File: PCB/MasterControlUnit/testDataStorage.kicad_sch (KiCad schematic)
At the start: 11 parts, among them U10 APS6404L-3SQR-SN, U11 APS6404L-3SQR-SN, U12 APS6404L-3SQR-SN, U2 APS6404L-3SQR-SN, U3 APS6404L-3SQR-SN, U4 APS6404L-3SQR-SN, U5 LD1117S33TR_SOT223, U6 APS6404L-3SQR-SN, U7 APS6404L-3SQR-SN, U8 APS6404L-3SQR-SN, U9 APS6404L-3SQR-SN

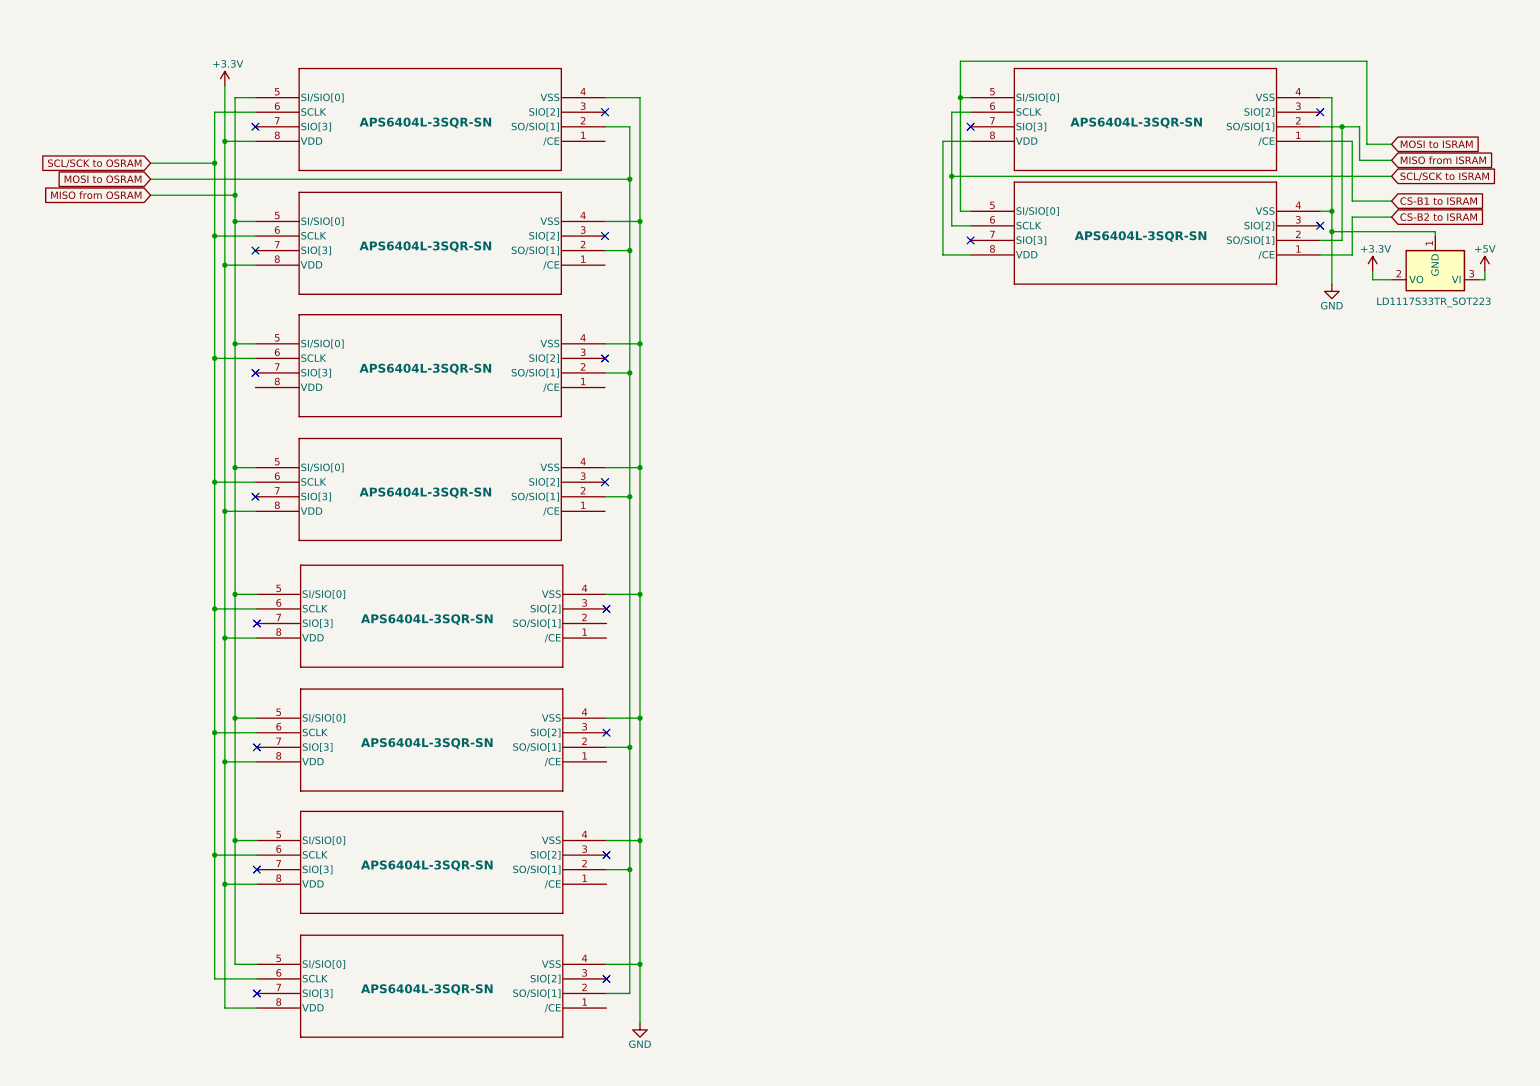
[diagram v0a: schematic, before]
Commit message: inputDataStorage.kicad_sch -> testDataStorage.kicad_sch
The cicuit of all SRAM (for bits-configurations or test's results) is defined un the testDataStorage.kicad_sch file
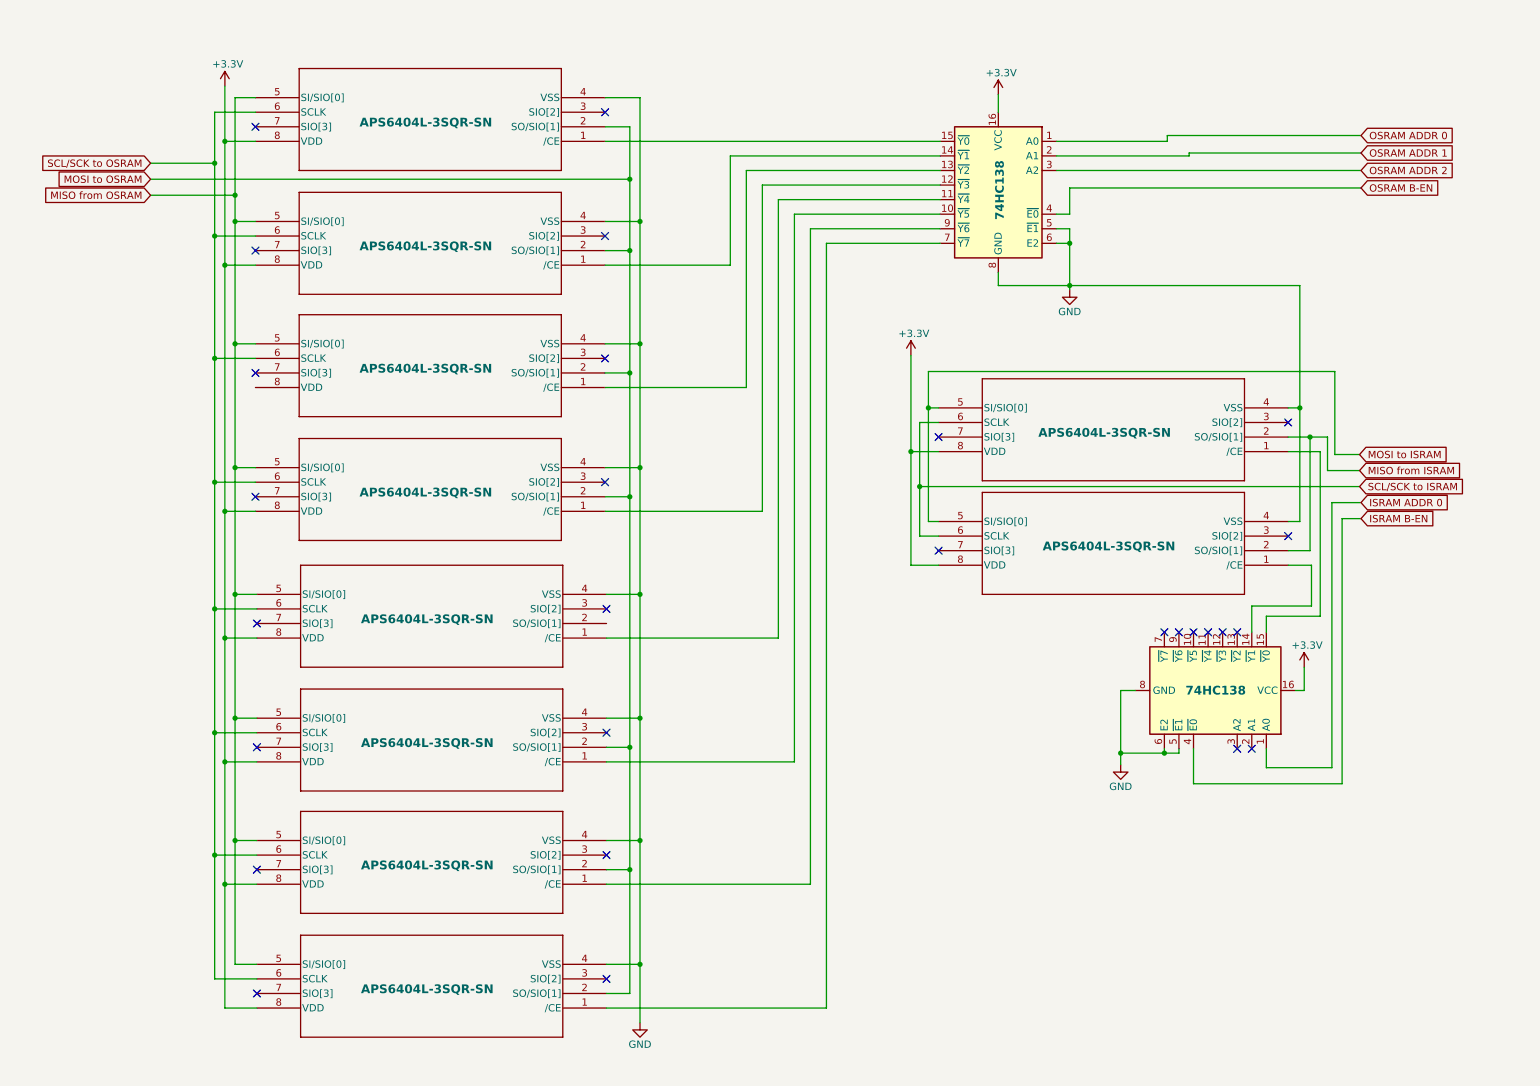
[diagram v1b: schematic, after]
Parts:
- removed U5: LD1117S33TR_SOT223, Package_TO_SOT_SMD:SOT-223-3_TabPin2, symbol Regulator_Linear:LD1117S33TR_SOT223
- added U13, U14: 74HC138, symbol 74xx:74HC138
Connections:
- net +3.3V: now also U2.8 (VDD), U3.8 (VDD), U13.16 (VCC), U14.16 (VCC)
- net GND: now also U13.5 (~{E1}), U13.6 (E2), U13.8 (GND), U14.5 (~{E1}), U14.6 (E2), U14.8 (GND)
- net at U4.1 (/CE): now also U13.15 (~{Y0})
- net at U7.1 (/CE): now also U13.13 (~{Y2})
- net at U9.1 (/CE): now also U13.11 (~{Y4})
- net at U12.1 (/CE): now also U13.7 (~{Y7})
- net at U8.1 (/CE): now also U13.12 (~{Y3})
- net at U10.1 (/CE): now also U13.10 (~{Y5})
- net at U6.1 (/CE): now also U13.14 (~{Y1})
- net at U11.1 (/CE): now also U13.9 (~{Y6})
- net CS-B1 to ISRAM: no longer names the net of U3.1 (/CE)
- net CS-B1 to ISRAM: now also U14.15 (~{Y0})
- net CS-B2 to ISRAM: no longer names the net of U2.1 (/CE)
- net CS-B2 to ISRAM: now also U14.14 (~{Y1})
- new net ISRAM ADDR 0: U14.1 (A0)
- new net ISRAM B-EN: U14.4 (~{E0})
- new net OSRAM ADDR 0: U13.1 (A0)
- new net OSRAM ADDR 1: U13.2 (A1)
- new net OSRAM ADDR 2: U13.3 (A2)
- new net OSRAM B-EN: U13.4 (~{E0})
- no-connect marks 20 -> 28

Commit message: Components footprints configured
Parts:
- U10, U11, U12, U2, U3, U4, U6, U7, U8, U9: footprint APS6404L-3SQR-SN_APY -> APS6404L-3SQR-SN:APS6404L-3SQR-SN_APY
- U13, U14: footprint (none) -> 74HC138:SOIC127P600X175-16N
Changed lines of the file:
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@@
 			)
 		)
-		(property "Footprint" "APS6404L-3SQR-SN_APY"
+		(property "Footprint" "APS6404L-3SQR-SN:APS6404L-3SQR-SN_APY"
 			(at 121.666 35.56 0)
 			(effects
@@
 			)
 		)
-		(property "Footprint" ""
+		(property "Footprint" "74HC138:SOIC127P600X175-16N"
 			(at 226.822 131.318 0)
 			(effects
@@
 			)
 		)
-		(property "Footprint" "APS6404L-3SQR-SN_APY"
+		(property "Footprint" "APS6404L-3SQR-SN:APS6404L-3SQR-SN_APY"
 			(at 121.666 78.486 0)
 			(effects
@@
 			)
 		)
-		(property "Footprint" "APS6404L-3SQR-SN_APY"
+		(property "Footprint" "APS6404L-3SQR-SN:APS6404L-3SQR-SN_APY"
 			(at 240.792 89.662 0)
 			(effects
@@
 			)
 		)
-		(property "Footprint" "APS6404L-3SQR-SN_APY"
+		(property "Footprint" "APS6404L-3SQR-SN:APS6404L-3SQR-SN_APY"
 			(at 121.92 122.174 0)
 			(effects
@@
 			)
 		)
-		(property "Footprint" "APS6404L-3SQR-SN_APY"
+		(property "Footprint" "APS6404L-3SQR-SN:APS6404L-3SQR-SN_APY"
 			(at 121.92 186.69 0)
 			(effects
@@
 			)
 		)
-		(property "Footprint" ""
+		(property "Footprint" "74HC138:SOIC127P600X175-16N"
 			(at 190.246 45.72 0)
 			(effects
@@
 			)
 		)
-		(property "Footprint" "APS6404L-3SQR-SN_APY"
+		(property "Footprint" "APS6404L-3SQR-SN:APS6404L-3SQR-SN_APY"
 			(at 121.666 100.076 0)
 			(effects
@@
 			)
 		)
-		(property "Footprint" "APS6404L-3SQR-SN_APY"
+		(property "Footprint" "APS6404L-3SQR-SN:APS6404L-3SQR-SN_APY"
 			(at 121.92 143.764 0)
 			(effects
@@
 			)
 		)
-		(property "Footprint" "APS6404L-3SQR-SN_APY"
+		(property "Footprint" "APS6404L-3SQR-SN:APS6404L-3SQR-SN_APY"
 			(at 121.666 57.15 0)
 			(effects
@@
 			)
 		)
-		(property "Footprint" "APS6404L-3SQR-SN_APY"
+		(property "Footprint" "APS6404L-3SQR-SN:APS6404L-3SQR-SN_APY"
 			(at 240.792 109.474 0)
 			(effects
@@
 			)
 		)
-		(property "Footprint" "APS6404L-3SQR-SN_APY"
+		(property "Footprint" "APS6404L-3SQR-SN:APS6404L-3SQR-SN_APY"
 			(at 121.92 165.1 0)
 			(effects

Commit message: Wrong label and unconnected pin fixed
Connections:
- net +3.3V: now also U7.8 (VDD)
- net MOSI to OSRAM: now also U9.2 (SO/SIO[1])
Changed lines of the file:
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@@
+	)
+	(junction
+		(at 125.984 119.634)
+		(diameter 0)
+		(color 0 0 0 0)
 	)
 	(junction
@@
 	)
 	(junction
+		(at 55.372 78.486)
+		(diameter 0)
+		(color 0 0 0 0)
+	)
+	(junction
 		(at 55.372 165.1)
 		(diameter 0)
@@
 	(wire
 		(pts
+			(xy 121.92 119.634) (xy 125.984 119.634)
+		)
+		(stroke
+			(width 0)
+			(type default)
+		)
+	)
+	(wire
+		(pts
 			(xy 57.15 114.554) (xy 57.15 92.456)
 		)
@@
 	(wire
 		(pts
-			(xy 125.984 97.536) (xy 125.984 141.224)
+			(xy 125.984 97.536) (xy 125.984 119.634)
 		)
 		(stroke
@@
 	(wire
 		(pts
+			(xy 55.372 78.486) (xy 60.706 78.486)
+		)
+		(stroke
+			(width 0)
+			(type default)
+		)
+	)
+	(wire
+		(pts
 			(xy 55.372 57.15) (xy 60.706 57.15)
 		)
@@
 	(wire
 		(pts
+			(xy 125.984 119.634) (xy 125.984 141.224)
+		)
+		(stroke
+			(width 0)
+			(type default)
+		)
+	)
+	(wire
+		(pts
 			(xy 175.006 72.898) (xy 175.006 89.662)
 		)
@@
 	(wire
 		(pts
+			(xy 55.372 78.486) (xy 55.372 100.076)
+		)
+		(stroke
+			(width 0)
+			(type default)
+		)
+	)
+	(wire
+		(pts
 			(xy 178.054 101.854) (xy 178.054 82.042)
 		)
@@
 	(wire
 		(pts
-			(xy 55.372 57.15) (xy 55.372 100.076)
-		)
-		(stroke
+			(xy 55.372 57.15) (xy 55.372 78.486)
+		)
+		(stroke

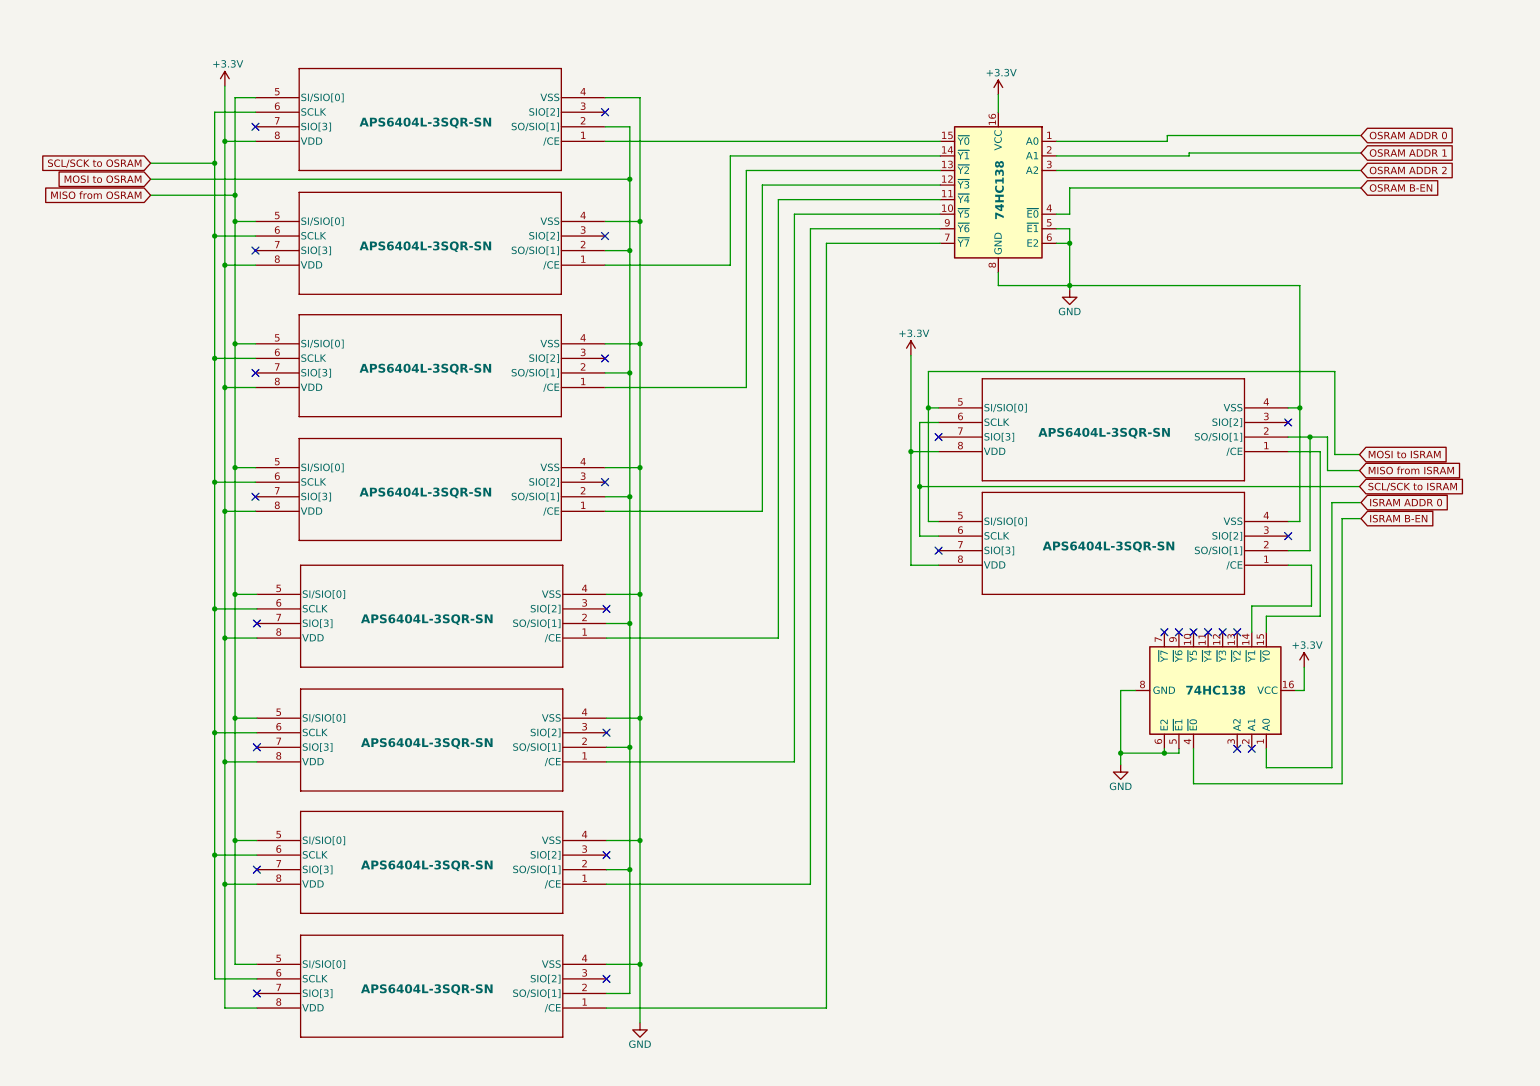
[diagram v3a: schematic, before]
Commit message: Add PSRAM decoupling capacitors, improve grounding and refine PCB routing
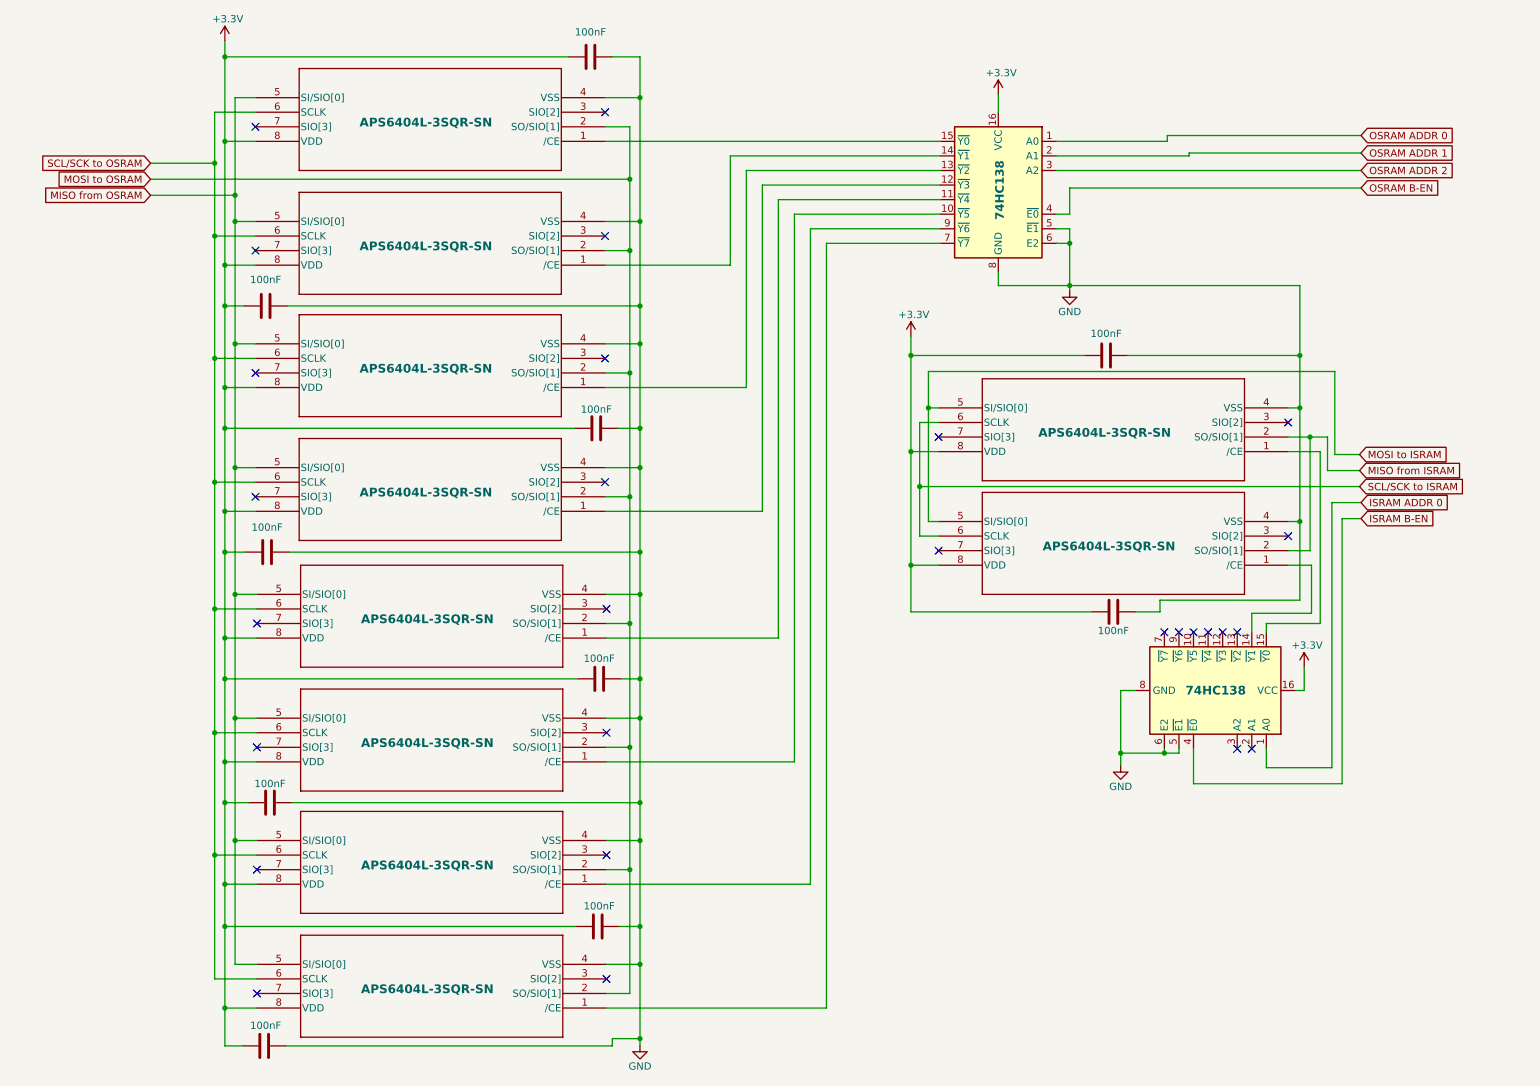
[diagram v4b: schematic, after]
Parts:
- added C10, C11, C12, C3, C4, C5, C6, C7, C8, C9: 100nF, Capacitor_SMD:C_1206_3216Metric, symbol Device:C
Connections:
- net +3.3V: now also C10.1, C11.1, C12.1, C3.1, C4.1, C5.1, C6.1, C7.1, C8.1, C9.1
- net GND: now also C10.2, C11.2, C12.2, C3.2, C4.2, C5.2, C6.2, C7.2, C8.2, C9.2
